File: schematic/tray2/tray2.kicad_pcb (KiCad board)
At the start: 2 copper layers, 52.1 x 100.3 mm, 62 parts, among them J1 AVR-ISP-10, J2 Conn_02x10_Odd_Even, J3 Conn_Coaxial, J4 Conn_Coaxial, J5 Conn_Coaxial, Q1 BF998, Q2 BFP196, Q3 BFR92A, Q4 BFR92A, Q5 BFR92A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

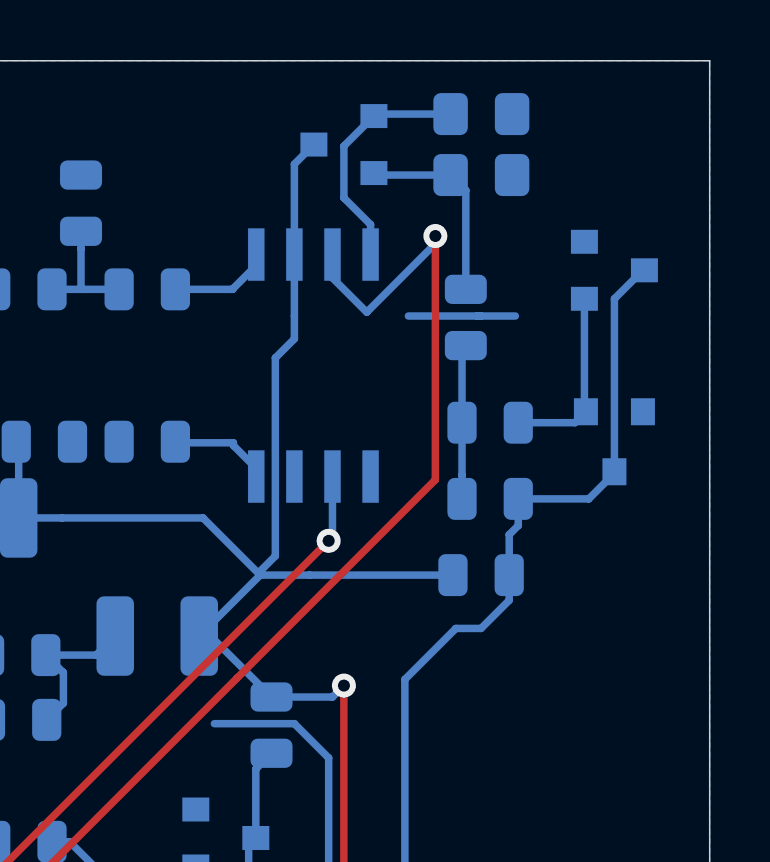
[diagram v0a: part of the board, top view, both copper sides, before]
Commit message: Move components so they don't mashup with holding rail
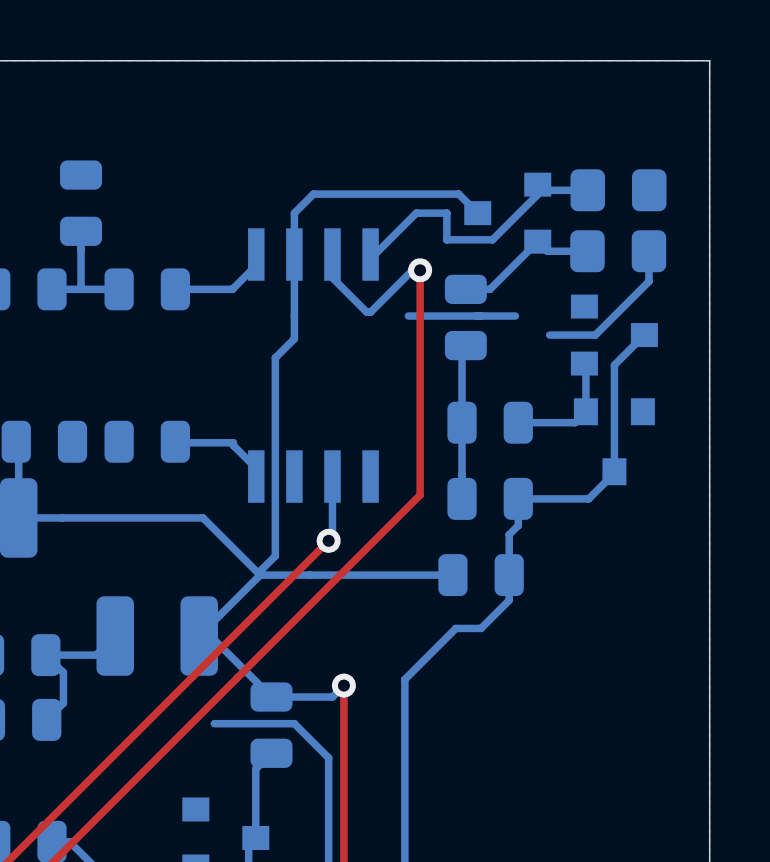
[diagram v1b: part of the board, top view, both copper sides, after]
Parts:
- moved Q5 5.92 mm to (69.5, 95.2)
- moved R19 5.23 mm to (73.2, 94.5)
- moved R20 5.22 mm to (73.2, 96.5)
- moved D3 2.16 mm to (73.0, 99.3)
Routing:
- net GND: track 61.3 -> 66.4 mm
- net VCC: track 221.7 -> 225.8 mm
- net PC0: track 97.1 -> 94.6 mm
- net Net-(D3-Pad3): track 46.0 -> 43.8 mm
- net Net-(D3-Pad1): track 6.19 -> 4.10 mm
- net Net-(C5-Pad2): track 6.60 -> 4.85 mm
- net Net-(Q5-Pad1): track 7.98 -> 9.73 mm
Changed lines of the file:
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@@
     (thickness 1.6)
     (drawings 6)
-    (tracks 444)
+    (tracks 454)
     (zones 0)
     (modules 62)
@@
   )
   (module Resistor_SMD:R_0805_2012Metric_Pad1.15x1.40mm_HandSolder (layer B.Cu)
-    (at 68.589 93.98)
+    (at 73.152 96.52)
     (descr "Resistor SMD 0805 (2012 Metric), square (rectangular) end terminal, IPC_7351 nominal with elongated pad for handsoldering. (Body size source: https://docs.google.com/spreadsheets/d/1BsfQQcO9C6DZCsRaXUlFlo91Tg2WpOkGARC1WS5S8t0/edit?usp=sharing), generated with kicad-footprint-generator")
     (tags "resistor handsolder")
@@
   )
   (module Resistor_SMD:R_0805_2012Metric_Pad1.15x1.40mm_HandSolder (layer B.Cu)
-    (at 68.589 91.948)
+    (at 73.161 94.488)
     (descr "Resistor SMD 0805 (2012 Metric), square (rectangular) end terminal, IPC_7351 nominal with elongated pad for handsoldering. (Body size source: https://docs.google.com/spreadsheets/d/1BsfQQcO9C6DZCsRaXUlFlo91Tg2WpOkGARC1WS5S8t0/edit?usp=sharing), generated with kicad-footprint-generator")
     (tags "resistor handsolder")
@@
   )
   (module Package_TO_SOT_SMD:SOT-23 (layer B.Cu)
-    (at 64.008 92.964 180)
+    (at 69.469 95.25 180)
     (descr "SOT-23, Standard")
     (tags SOT-23)
@@
   )
   (module Package_TO_SOT_SMD:SOT-23 (layer B.Cu)
-    (at 73.025 97.155)
+    (at 73.025 99.314)
     (descr "SOT-23, Standard")
     (tags SOT-23)
@@
   (segment (start 68.453 98.679) (end 68.58 98.679) (width 0.25) (layer B.Cu) (net 1))
   (segment (start 66.15665 98.679) (end 68.453 98.679) (width 0.25) (layer B.Cu) (net 1))
+  (segment (start 74.177 97.527) (end 74.177 96.52) (width 0.25) (layer B.Cu) (net 1))
+  (segment (start 70.866 99.314) (end 72.39 99.314) (width 0.25) (layer B.Cu) (net 1))
+  (segment (start 72.39 99.314) (end 74.177 97.527) (width 0.25) (layer B.Cu) (net 1))
   (segment (start 46.355 142.5725) (end 46.355 139.33) (width 0.25) (layer B.Cu) (net 2))
   (segment (start 46.6875 142.24) (end 46.355 142.5725) (width 0.25) (layer B.Cu) (net 2))
@@
   (segment (start 55.656 121.158) (end 55.783 121.285) (width 0.25) (layer B.Cu) (net 7))
   (segment (start 55.656 118.872) (end 55.656 121.158) (width 0.25) (layer B.Cu) (net 7))
-  (segment (start 65.074 93.98) (end 65.008 93.914) (width 0.25) (layer B.Cu) (net 8))
-  (segment (start 67.564 93.98) (end 65.074 93.98) (width 0.25) (layer B.Cu) (net 8))
-  (segment (start 68.072 94.488) (end 67.564 93.98) (width 0.25) (layer B.Cu) (net 8))
-  (segment (start 68.072 97.79) (end 68.072 94.488) (width 0.25) (layer B.Cu) (net 8))
+  (segment (start 70.789 96.52) (end 70.469 96.2) (width 0.25) (layer B.Cu) (net 8))
+  (segment (start 72.127 96.52) (end 70.789 96.52) (width 0.25) (layer B.Cu) (net 8))
+  (segment (start 68.879 97.79) (end 70.469 96.2) (width 0.25) (layer B.Cu) (net 8))
+  (segment (start 68.072 97.79) (end 68.879 97.79) (width 0.25) (layer B.Cu) (net 8))
   (segment (start 67.945 103.975) (end 67.945 102.235) (width 0.25) (layer B.Cu) (net 9))
   (segment (start 67.945 104.775) (end 67.945 103.975) (width 0.25) (layer B.Cu) (net 9))
@@
   (segment (start 72.17 104.775) (end 73.025 103.92) (width 0.25) (layer B.Cu) (net 22))
   (segment (start 69.82 104.775) (end 72.17 104.775) (width 0.25) (layer B.Cu) (net 22))
-  (segment (start 73.975 97.155) (end 74.025 97.155) (width 0.25) (layer B.Cu) (net 22))
-  (segment (start 73.025 98.105) (end 73.975 97.155) (width 0.25) (layer B.Cu) (net 22))
-  (segment (start 73.025 103.87) (end 73.025 98.105) (width 0.25) (layer B.Cu) (net 22))
   (segment (start 68.58 109.093) (end 69.5175 108.1555) (width 0.25) (layer B.Cu) (net 22))
   (segment (start 67.7395 109.093) (end 68.58 109.093) (width 0.25) (layer B.Cu) (net 22))
@@
   (segment (start 69.82 105.664) (end 69.82 104.775) (width 0.25) (layer B.Cu) (net 22))
   (segment (start 69.5175 105.9665) (end 69.82 105.664) (width 0.25) (layer B.Cu) (net 22))
+  (segment (start 73.025 100.314) (end 74.025 99.314) (width 0.25) (layer B.Cu) (net 22))
+  (segment (start 73.025 103.87) (end 73.025 100.314) (width 0.25) (layer B.Cu) (net 22))
   (segment (start 72.025 101.82) (end 72.075 101.87) (width 0.25) (layer B.Cu) (net 24))
-  (segment (start 72.025 98.105) (end 72.025 101.82) (width 0.25) (layer B.Cu) (net 24))
   (segment (start 71.71 102.235) (end 72.075 101.87) (width 0.25) (layer B.Cu) (net 24))
   (segment (start 69.82 102.235) (end 71.71 102.235) (width 0.25) (layer B.Cu) (net 24))
+  (segment (start 72.075 100.314) (end 72.025 100.264) (width 0.25) (layer B.Cu) (net 24))
+  (segment (start 72.075 101.87) (end 72.075 100.314) (width 0.25) (layer B.Cu) (net 24))
   (segment (start 62.23 141.605) (end 62.23 142.875) (width 0.25) (layer B.Cu) (net 25))
   (segment (start 62.26001 141.57499) (end 62.23 141.605) (width 0.25) (layer B.Cu) (net 25))
@@
   (segment (start 61.722 100.076) (end 61.722 106.68) (width 0.25) (layer B.Cu) (net 29))
   (segment (start 61.722 106.68) (end 61.214 107.188) (width 0.25) (layer B.Cu) (net 29))
-  (segment (start 62.357 93.615) (end 63.008 92.964) (width 0.25) (layer B.Cu) (net 29))
-  (segment (start 62.357 96.63) (end 62.357 93.615) (width 0.25) (layer B.Cu) (net 29))
+  (segment (start 67.834 94.615) (end 68.469 95.25) (width 0.25) (layer B.Cu) (net 29))
+  (segment (start 62.992 94.615) (end 67.834 94.615) (width 0.25) (layer B.Cu) (net 29))
+  (segment (start 62.357 96.63) (end 62.357 95.25) (width 0.25) (layer B.Cu) (net 29))
+  (segment (start 62.357 95.25) (end 62.992 94.615) (width 0.25) (layer B.Cu) (net 29))
   (segment (start 56.32 170.275) (end 60.23 170.275) (width 0.25) (layer B.Cu) (net 30))
   (segment (start 60.5325 170.275) (end 60.23 170.275) (width 0.25) (layer B.Cu) (net 30))
@@
   (segment (start 46.8921 158.3473) (end 44.6278 158.3473) (width 0.25) (layer B.Cu) (net 83))
   (segment (start 47.0027 158.4579) (end 46.8921 158.3473) (width 0.25) (layer B.Cu) (net 83))
-  (segment (start 65.074 91.948) (end 65.008 92.014) (width 0.25) (layer B.Cu) (net 84))
-  (segment (start 67.564 91.948) (end 65.074 91.948) (width 0.25) (layer B.Cu) (net 84))
-  (segment (start 64.897 96.63) (end 64.897 95.631) (width 0.25) (layer B.Cu) (net 84))
-  (segment (start 64.897 95.631) (end 64.008 94.742) (width 0.25) (layer B.Cu) (net 84))
-  (segment (start 64.008 93.014) (end 65.008 92.014) (width 0.25) (layer B.Cu) (net 84))
-  (segment (start 64.008 94.742) (end 64.008 93.014) (width 0.25) (layer B.Cu) (net 84))
+  (segment (start 64.897 96.63) (end 65.041 96.63) (width 0.25) (layer B.Cu) (net 84))
+  (segment (start 65.041 96.63) (end 66.421 95.25) (width 0.25) (layer B.Cu) (net 84))
+  (segment (start 66.421 95.25) (end 67.439999 95.25) (width 0.25) (layer B.Cu) (net 84))
+  (segment (start 67.439999 95.25) (end 67.439999 96.136001) (width 0.25) (layer B.Cu) (net 84))
+  (segment (start 67.439999 96.136001) (end 67.442998 96.139) (width 0.25) (layer B.Cu) (net 84))
+  (segment (start 67.442998 96.139) (end 68.961 96.139) (width 0.25) (layer B.Cu) (net 84))
+  (segment (start 70.469 94.631) (end 70.469 94.3) (width 0.25) (layer B.Cu) (net 84))
+  (segment (start 68.961 96.139) (end 70.469 94.631) (width 0.25) (layer B.Cu) (net 84))
+  (segment (start 70.657 94.488) (end 70.469 94.3) (width 0.25) (layer B.Cu) (net 84))
+  (segment (start 72.136 94.488) (end 70.657 94.488) (width 0.25) (layer B.Cu) (net 84))
   (segment (start 49.27 172.525) (end 49.27 173.984) (width 0.25) (layer B.Cu) (net 85))
   (via (at 49.27 173.984) (size 0.8) (drill 0.4) (layers F.Cu B.Cu) (net 85))
@@
   (segment (start 63.627 96.63) (end 63.627 97.409) (width 0.25) (layer B.Cu) (net 86))
   (segment (start 63.627 97.409) (end 64.77 98.552) (width 0.25) (layer B.Cu) (net 86))
-  (segment (start 64.77 98.552) (end 67.056 96.266) (width 0.25) (layer B.Cu) (net 86))
-  (via (at 67.056 96.012) (size 0.8) (drill 0.4) (layers F.Cu B.Cu) (net 86))
-  (segment (start 67.056 96.266) (end 67.056 96.012) (width 0.25) (layer B.Cu) (net 86))
-  (segment (start 67.056 96.012) (end 67.056 104.14) (width 0.25) (layer F.Cu) (net 86))
-  (segment (start 67.056 104.14) (end 60.452 110.744) (width 0.25) (layer F.Cu) (net 86))
   (segment (start 60.452 110.744) (end 45.72 125.476) (width 0.25) (layer F.Cu) (net 86))
   (segment (start 45.72 125.476) (end 45.72 159.766) (width 0.25) (layer F.Cu) (net 86))
@@
   (segment (start 50.07 173.514) (end 50.07 172.525) (width 0.25) (layer B.Cu) (net 86))
   (segment (start 50.546 173.99) (end 50.07 173.514) (width 0.25) (layer B.Cu) (net 86))
+  (segment (start 64.77 98.552) (end 64.897 98.552) (width 0.25) (layer B.Cu) (net 86))
+  (segment (start 64.897 98.552) (end 66.294 97.155) (width 0.25) (layer B.Cu) (net 86))
+  (segment (start 66.294 97.155) (end 66.548 97.155) (width 0.25) (layer B.Cu) (net 86))
+  (via (at 66.548 97.155) (size 0.8) (drill 0.4) (layers F.Cu B.Cu) (net 86))
+  (segment (start 66.548 97.155) (end 66.548 104.648) (width 0.25) (layer F.Cu) (net 86))
+  (segment (start 66.548 104.648) (end 60.452 110.744) (width 0.25) (layer F.Cu) (net 86))
   (zone (net 1) (net_name GND) (layer B.Cu) (hatch edge 0.508)
     (connect_pads (clearance 0.508))
